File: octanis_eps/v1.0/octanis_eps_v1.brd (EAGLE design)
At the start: 80 x 50 mm, 141 parts, among them IC1 OPA2333DGK, Q1 32.768kHz, Q100 BSS123, U1 CSD16327Q3_DQG_8, U10 CSD16327Q3_DQG_8, U100 Value, U11 CSD16327Q3_DQG_8, U2 CSD16327Q3_DQG_8, U3 CSD16327Q3_DQG_8, U4 MSP430G2544, U5 TPS2022D, U6 Value, U7 Value, U8 TPS61232, U9 BQ24650_RVA_16

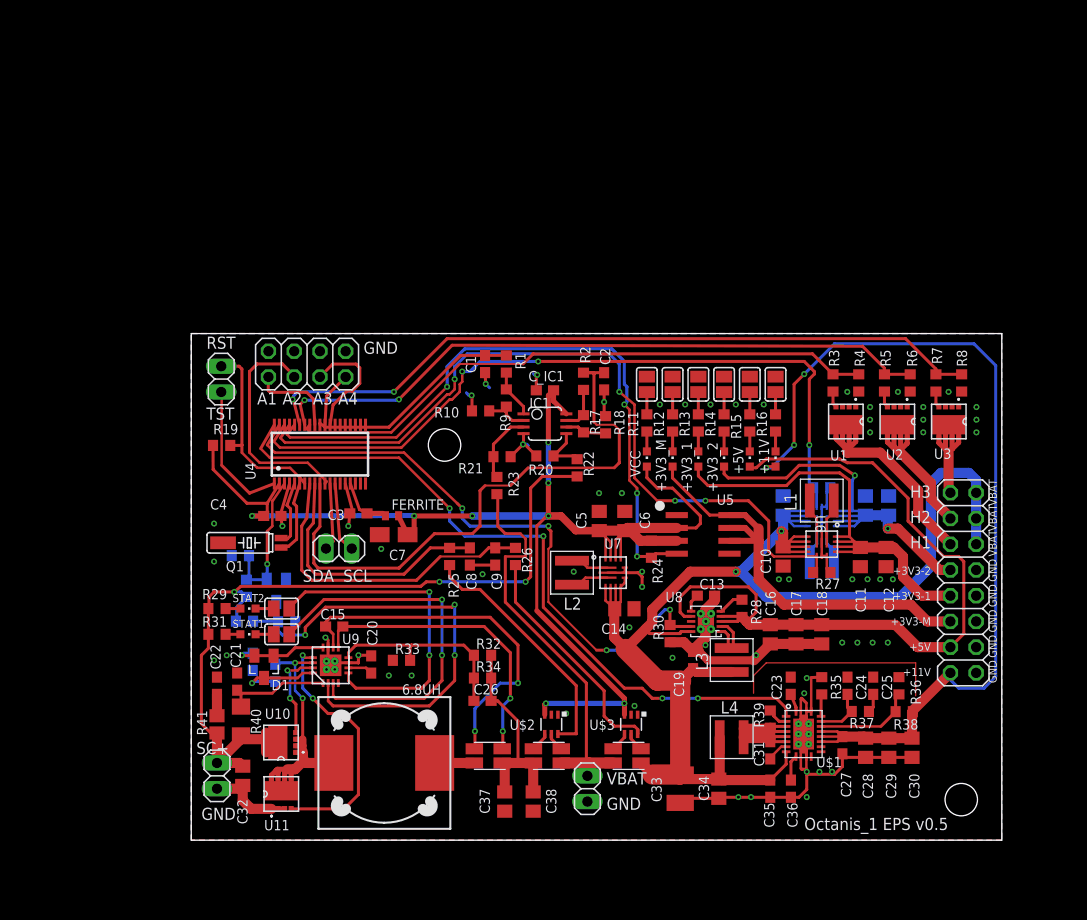
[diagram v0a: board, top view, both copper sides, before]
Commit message: restored old v0.5, renamed v1.0 correctly
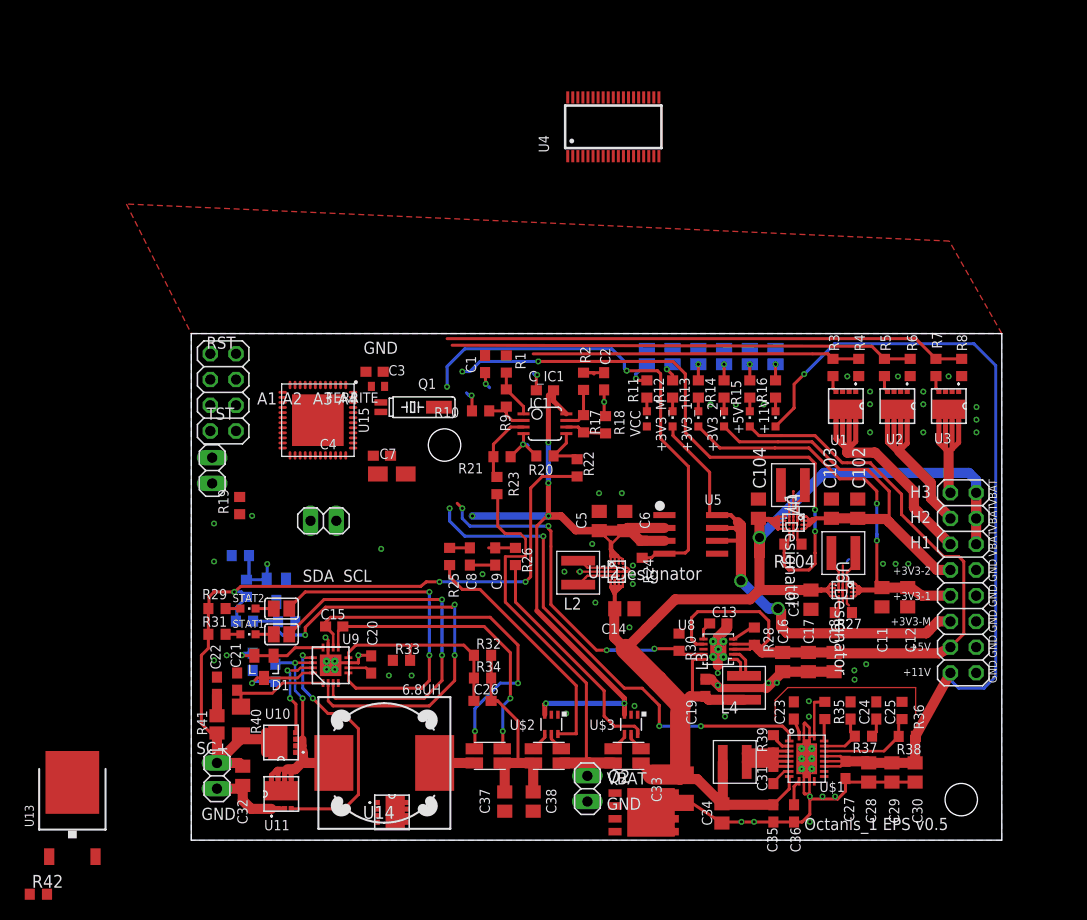
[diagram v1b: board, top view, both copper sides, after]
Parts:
- removed U100: Value, octanis_eps_v05:RNC0014A
- added Q2: BSC340N08NS3G, transistor-power:PG-TDSON-8
- added R42: dnp, resistor:R0603
- added U12: TPS630250YFFT, texasinstruments:YFF0020AEBA
- added U13: (no value), Seeed-OPL-ic:TO-252
- added U14: CSD16327Q3_DQG_8, texasinstruments:DQG8
- added U15: MSP430FR5969, chips:S-PVQFN-N48
- R35: value 270k -> 100k
- U6, U7: value Value -> TPS630250YFFT; device octanis_eps_v05:RNC0014A -> texasinstruments:YFF0020AEBA
- moved U4 43.4 mm to (41.7, 70.4)
- moved Q1 23.0 mm to (23.1, 42.7), turned to 270 degrees
- moved U7 18.5 mm to (59.4, 31.3), turned to 270 degrees
- moved C3 14.1 mm to (18.1, 46.2), turned to 0 degrees
- moved FERRITE 12.8 mm to (18.4, 44.8), turned to 0 degrees
- moved C4 12.3 mm to (18.8, 37.9)
- moved JP2 9.07 mm to (2.07, 36.5), turned to 90 degrees
- moved JP1 8.74 mm to (3.15, 44.2), turned to 90 degrees
- moved L100 8.12 mm to (59.4, 35.0), flipped to the top, turned to 0 degrees
- moved R104 6.26 mm to (59.4, 29.2), flipped to the top, turned to 0 degrees
- moved R19 6.20 mm to (4.78, 33.0), turned to 270 degrees
- moved C7 6.00 mm to (19.8, 36.1), turned to 180 degrees
- moved L1 5.60 mm to (64.4, 28.3)
- moved C10 5.07 mm to (61.2, 23.7)
- moved U6 4.98 mm to (64.3, 24.7)
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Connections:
- removed net N$30: Q1.P1, U4.6
- removed net N$36: Q1.P2, U4.5
- removed net N$75: JP2.2, U4.1
- removed net N$93: JP2.1, R19.1, U4.7
- removed net N$99: C3.1, FERRITE.2, U4.16
- new net AGND: C3.2, U15.41, U15.44, U15.47
- new net N$10: C3.1, FERRITE.1, U15.48
- new net N$13: JP2.1, R19.1, U15.23
- new net N$15: JP2.2, U15.22
- new net N$16: Q1.P1, U15.46
- new net N$17: Q1.P2, U15.45
- new net N$9: R42.1, U$1.P$13
- net +3V3: now also FERRITE.2, U12.1, U12.2, U12.3, U12.4, U15.37; no longer FERRITE.1, U4.2, U7.11, U7.12, U7.13, U7.14
- net +3V3_1: now also U6.1, U6.2, U6.3, U6.4; no longer U6.11, U6.12, U6.13, U6.14
- net +3V3_2: now also U7.1, U7.2, U7.3, U7.4; no longer U100.11, U100.12, U100.13, U100.14
- net A_EXT1: now also JP1.7, U15.16; no longer JP1.1, U4.30
- net A_EXT2: now also JP1.5, U15.17; no longer JP1.3, U4.11
- net A_EXT3: now also JP1.3, U15.18; no longer JP1.5, U4.27
- net A_EXT4: now also JP1.1, U15.19; no longer JP1.7, U4.28
- net BAT_OUT: now also U12.16, U12.17, U12.18, U12.19, U12.20, U6.17, U6.18, U6.19, U6.20, U7.17, U7.18, U7.19, U7.20; no longer U100.4, U100.5, U100.6, U100.7, U6.4, U6.5, U6.6, U6.7, U7.4, U7.5, U7.6, U7.7, U7.8
- net EN_12V: now also U15.28; no longer U4.38
- net EN_3V3_1: now also U15.34, U6.16; no longer U4.35, U6.8
- net EN_3V3_2: now also U15.35, U7.16; no longer U100.8, U4.36
- net EN_3V3_M: now also U15.33; no longer U4.34
- net EN_5V: now also U15.29; no longer U4.37
- net EN_SC: now also U15.27; no longer U4.3
- net GND: now also R42.2, U12.10, U12.11, U12.12, U12.8, U12.9, U15.36, U15.VSS_QFN, U6.11, U6.12, U6.8, U7.11, U7.12, U7.8; no longer C3.2, U100.10, U100.2, U100.9, U4.15, U4.4, U6.2, U7.2
- net I2C_SCL: now also U15.32; no longer U4.13
- net I2C_SDA: now also U15.31; no longer U4.12
- net I_IN: now also U15.2; no longer U4.9
- net I_OUT: now also U15.1; no longer U4.8
- net N$1: now also U12.13, U12.14, U12.15; no longer U7.3
- net N$11: now also U7.13, U7.14, U7.15; no longer U100.3
- net N$12: now also U7.5, U7.6, U7.7; no longer U100.1
- net N$3: now also U12.5, U12.6, U12.7; no longer U7.1
- net N$6: now also U6.13, U6.14, U6.15; no longer U6.3
- net N$7: now also U6.5, U6.6, U6.7; no longer U6.1
- net V_BAT: now also U15.9; no longer U4.29
- net V_SC: now also U15.3; no longer U4.10
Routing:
- net EN_3V3_1: track 77.3 -> 1.80 mm, vias 4 -> 0
- net V_SC: track 58.7 -> 3.12 mm
- net +3V3: track 140.3 -> 86.3 mm, vias 8 -> 7
- net I_OUT: track 31.5 -> 2.65 mm
- net EN_HEAT1: track 59.2 -> 32.3 mm
- net I_IN: track 25.8 -> 2.00 mm
- net EN_5V: track 60.9 -> 37.6 mm
- net A_EXT2: track 22.4 -> 0.00 mm
- net V_BAT: track 21.6 -> 0.00 mm
- net EN_HEAT3: track 73.0 -> 51.6 mm, vias 2 -> 0
- net EN_12V: track 70.8 -> 49.5 mm
- net EN_HEAT2: track 66.2 -> 45.7 mm, vias 2 -> 0
- net N$93: track 19.1 -> 0.00 mm
- net EN_3V3_M: track 64.1 -> 48.6 mm, vias 4 -> 2
- net EN_3V3_2: track 74.5 -> 60.0 mm, vias 3 -> 4
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
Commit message: now all EPS components are on top side
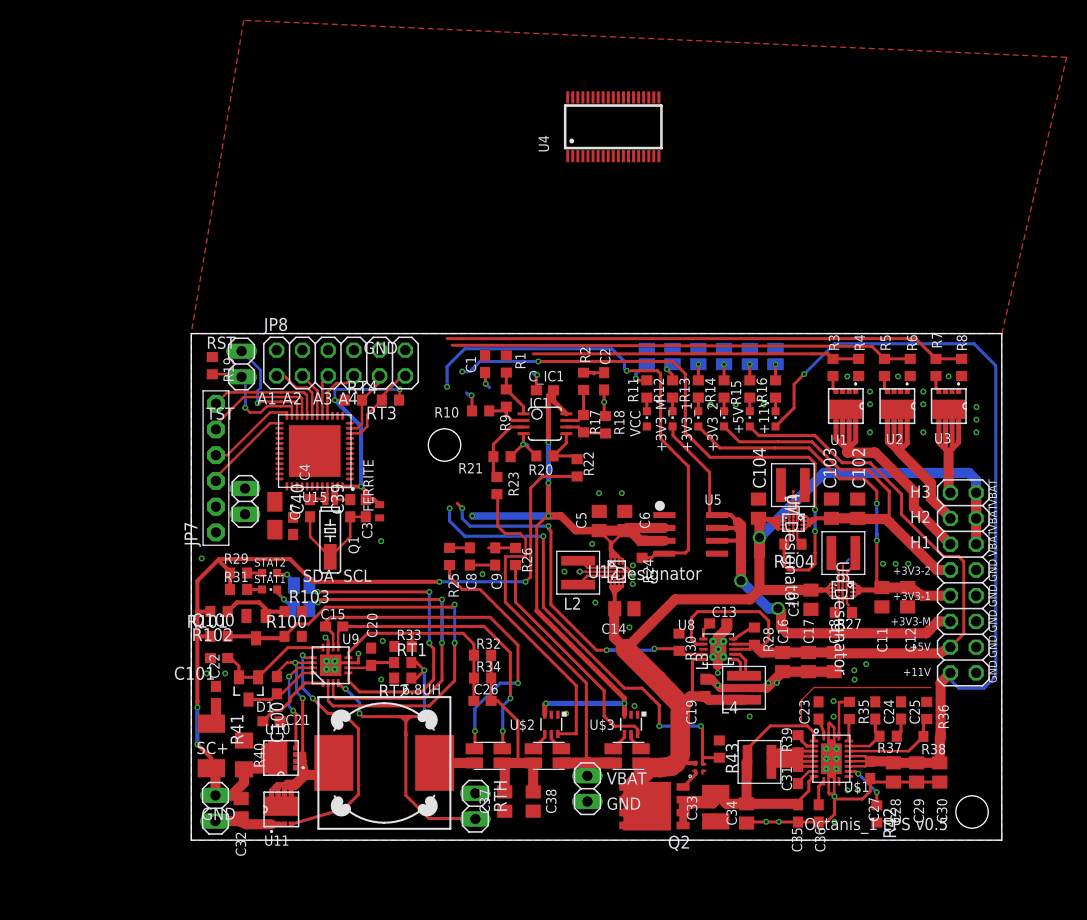
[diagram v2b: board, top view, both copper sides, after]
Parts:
- removed JP1: (no value), Headerlibrary:2X04
- removed U13: (no value), Seeed-OPL-ic:TO-252
- removed U14: CSD16327Q3_DQG_8, texasinstruments:DQG8
- added C39, C40: 12pF, rcl:C0603
- added JP7: (no value), adafruit:1X06-BIG
- added JP8: (no value), Headerlibrary:2X06
- added R43: 1M, rcl:R0603
- added RT1, RT3, RT4: 2723, rcl:R0603
- added RT2: 8501, rcl:R0603
- added RTH: (no value), Headerlibrary:1X02
- added U$4: MIC4414, Octanis1_EPS:QFN-4
- Q2: value BSC340N08NS3G -> BSC0901NS
- R41: device rcl:R2012 -> rcl:R2010
- moved R42 83.1 mm to (67.7, 2.59), turned to 270 degrees
- moved Q1 16.4 mm to (13.7, 29.3), turned to 180 degrees
- moved R19 14.1 mm to (2.08, 46.8), turned to 90 degrees
- moved C3 13.5 mm to (17.2, 32.8), turned to 270 degrees
- moved FERRITE 12.3 mm to (18.6, 32.5), turned to 270 degrees
- moved C7 12.3 mm to (8.25, 32.0), turned to 90 degrees
- moved C4 11.2 mm to (10.1, 31.0), turned to 270 degrees
- moved JP2 10.9 mm to (4.96, 47.0)
- moved JP3 7.97 mm to (5.31, 33.4), turned to 270 degrees
- moved R103 7.59 mm to (10.1, 22.6), flipped to the top
- moved C21 5.18 mm to (7.92, 11.7), turned to 0 degrees
- moved R31 4.91 mm to (4.67, 24.7)
- moved STAT1 4.91 mm to (7.73, 24.7)
- moved R29 4.10 mm to (4.67, 26.4)
- moved STAT2 4.10 mm to (7.73, 26.4)
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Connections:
- new net A4_EXT: JP8.11, RT3.2, U15.10
- new net A5_EXT: JP8.9, RT4.2, U15.11
- new net AVCC: C3.1, FERRITE.1, RT3.1, RT4.1, U15.48
- new net BAT_11V: C33.1, C34.1, C35.1, L4.P$1, Q2.1, Q2.2, Q2.3, U$1.P$2, U$1.P$9
- new net N$18: JP7.3, U15.25
- new net N$28: JP7.4, U15.24
- new net N$29: JP7.2, U15.39
- new net N$30: JP7.1, U15.40
- new net N$36: JP7.5, U15.21
- new net N$41: JP7.6, U15.20
- new net TS: RT1.2, RT2.1, RTH.2, U9.4
- net AGND: now also C39.1, C40.1, JP8.10, JP8.12, JP8.2, JP8.4, JP8.6, JP8.8, Q1.P3
- net A_EXT1: now also JP8.7; no longer JP1.7
- net A_EXT2: now also JP8.5; no longer JP1.5
- net A_EXT3: now also JP8.3; no longer JP1.3
- net A_EXT4: now also JP8.1; no longer JP1.1
- net BAT_OUT: now also Q2.5, Q2.6, Q2.7, Q2.8, U$4.P$4, U$4.P4; no longer C33.1, C34.1, C35.1, L4.P$1, U$1.P$9
- net EN_12V: now also R43.2, U$4.P$3, U$4.P3; no longer U$1.P$2
- net GND: now also R43.1, RT2.2, RTH.1, U$4.P$2, U$4.P2; no longer JP1.2, JP1.4, JP1.6, JP1.8, Q1.P3
- net N$10: now also Q2.4, U$4.P$1, U$4.P1; no longer C3.1, FERRITE.1, U15.48
- net N$16: now also C39.2
- net N$17: now also C40.2
- net N$72: now also RT1.1
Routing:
- net BAT_11V: track 0.00 -> 37.4 mm
- net TS: track 0.00 -> 36.3 mm, vias 0 -> 4
- net AVCC: track 0.00 -> 24.0 mm, vias 0 -> 3
- net N$13: track 0.00 -> 12.2 mm, vias 0 -> 1
- net N$36: track 0.00 -> 11.9 mm
- net N$41: track 0.00 -> 11.6 mm
- net N$15: track 0.00 -> 11.4 mm, vias 0 -> 1
- net AGND: track 0.00 -> 11.1 mm
- net BAT_OUT: track 141.8 -> 131.9 mm
- net N$28: track 0.00 -> 9.09 mm
- net A4_EXT: track 0.00 -> 8.85 mm
- net N$18: track 0.00 -> 8.85 mm
- net GND: track 119.6 -> 111.9 mm, vias 61 -> 60
- net A5_EXT: track 0.00 -> 6.82 mm
- net A_EXT4: track 0.00 -> 6.47 mm
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
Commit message: finished component placement of new EPS
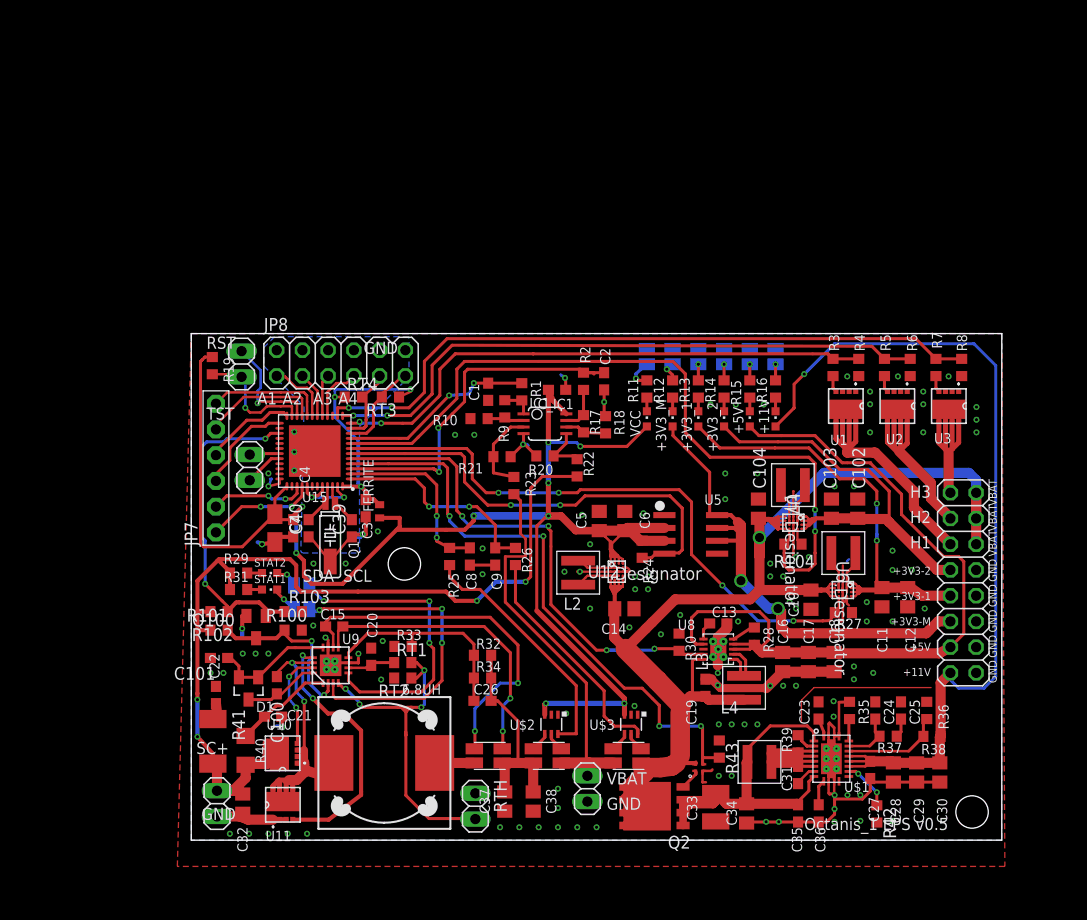
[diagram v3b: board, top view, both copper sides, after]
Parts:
- removed U4: MSP430G2544, Octanis1_EPS:TSSOP38
- moved JP3 3.38 mm to (5.77, 36.8)
- moved R1 3.14 mm to (32.6, 44.3)
- moved C1 2.76 mm to (29.3, 44.3)
- moved C39 1.99 mm to (15.8, 30.8)
- moved C40 1.99 mm to (11.6, 30.8)
- moved R23 1.68 mm to (31.8, 35.0)
- moved C7 1.22 mm to (8.25, 30.8)
- moved C_IC1 1.20 mm to (36.1, 44.4), turned to 180 degrees
- moved R9 1.08 mm to (30.9, 42.6)
- moved R10 0.78 mm to (28.4, 41.6)
- moved R100 0.61 mm to (10.1, 20.7)
- moved R101 0.61 mm to (2.74, 20.7)
- moved R40 0.48 mm to (5.37, 8.86)
- moved U10 0.48 mm to (9.01, 8.57)
- moved R41 0.48 mm to (2.13, 9.75)
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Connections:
- net EN_12V: now also U15.4; no longer U15.28
- net EN_3V3_1: now also U15.7; no longer U15.34
- net EN_3V3_2: now also U15.8; no longer U15.35
- net EN_3V3_M: now also U15.6; no longer U15.33
- net EN_5V: now also U15.5; no longer U15.29
- net EN_HEAT1: now also U15.12; no longer U4.31
- net EN_HEAT2: now also U15.13; no longer U4.32
- net EN_HEAT3: now also U15.14; no longer U4.33
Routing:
- net +3V3: track 86.3 -> 162.7 mm, vias 6 -> 9
- net EN_3V3_1: track 1.80 -> 61.9 mm, vias 0 -> 4
- net V_SC: track 3.12 -> 35.6 mm, vias 0 -> 2
- net N$64: track 47.1 -> 18.0 mm
- net EN_SC: track 7.13 -> 32.7 mm, vias 0 -> 2
- net EN_HEAT1: track 32.3 -> 55.0 mm, vias 0 -> 2
- net V_BAT: track 0.00 -> 19.5 mm, vias 0 -> 2
- net GND: track 111.9 -> 131.4 mm, vias 60 -> 117
- net I_OUT: track 2.65 -> 21.3 mm, vias 0 -> 2
- net EN_HEAT3: track 51.6 -> 67.8 mm, vias 0 -> 2
- net I_IN: track 2.00 -> 18.0 mm, vias 0 -> 2
- net EN_3V3_2: track 60.0 -> 75.7 mm, vias 4 -> 2
- net EN_HEAT2: track 45.7 -> 61.1 mm, vias 0 -> 2
- net EN_5V: track 37.6 -> 52.1 mm
- net EN_12V: track 45.3 -> 59.2 mm
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- added copper zone on layer 16, net AGND

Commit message: dru check; added proper grounding and AVCC for all amps
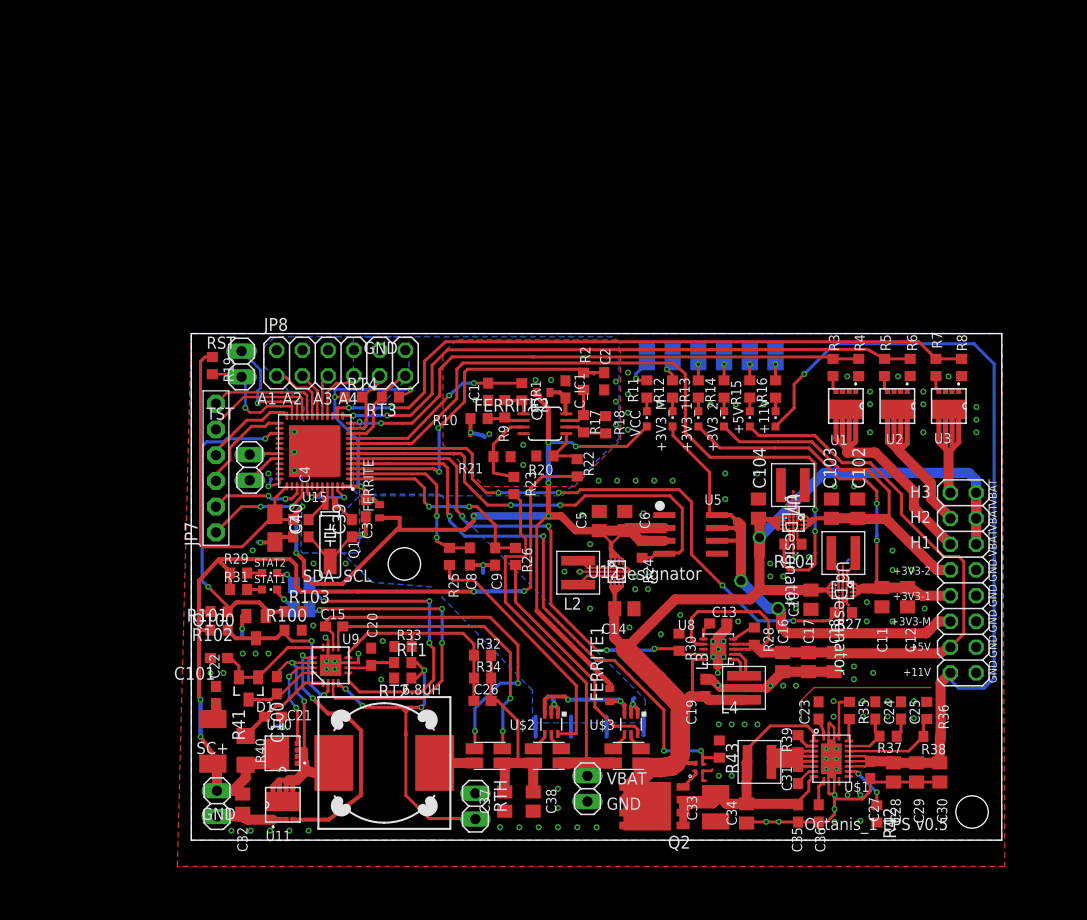
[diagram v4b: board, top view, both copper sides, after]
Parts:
- added FERRITE1, FERRITE2: 100mH, inductors:0402
- moved C_IC1 0.83 mm to (36.9, 44.5), turned to 270 degrees
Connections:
- new net AVCC1: FERRITE1.1, U$2.3, U$3.3
- new net AVCC2: C_IC1.2, FERRITE2.1, IC1.8
- net +3V3: now also FERRITE1.2, FERRITE2.2; no longer C_IC1.2, IC1.8, U$2.3, U$3.3
- net AGND: now also C1.1, C2.1, C8.1, C9.1, C_IC1.1, IC1.4, R10.2, R18.2, R20.1, R21.1, U$2.1, U$2.2, U$3.1, U$3.2
- net GND: no longer C1.1, C2.1, C8.1, C9.1, C_IC1.1, IC1.4, R10.2, R18.2, R20.1, R21.1, U$2.1, U$2.2, U$3.1, U$3.2
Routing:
- net AGND: track 19.7 -> 36.5 mm, vias 3 -> 16
- net +3V3: track 162.7 -> 148.0 mm, vias 9 -> 7
- net AVCC1: track 0.00 -> 11.9 mm, vias 0 -> 2
- net GND: track 131.4 -> 122.7 mm, vias 117 -> 123
- net AVCC2: track 0.00 -> 3.37 mm
- net SC+: track 89.1 -> 88.6 mm
- added copper zone on layer 1, net AGND
